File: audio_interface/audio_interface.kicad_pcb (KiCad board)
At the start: 2 copper layers, 137.8 x 66 mm, 153 parts, among them J1 XLR3, J10 MIC_EXT, J11 INST_EXT, J13 Test Headers, J14 SWD, J15 PCM_Jumper, J16 USB_B, J2 AudioJack2, J3 EXT_9V, J4 PROBE_GND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

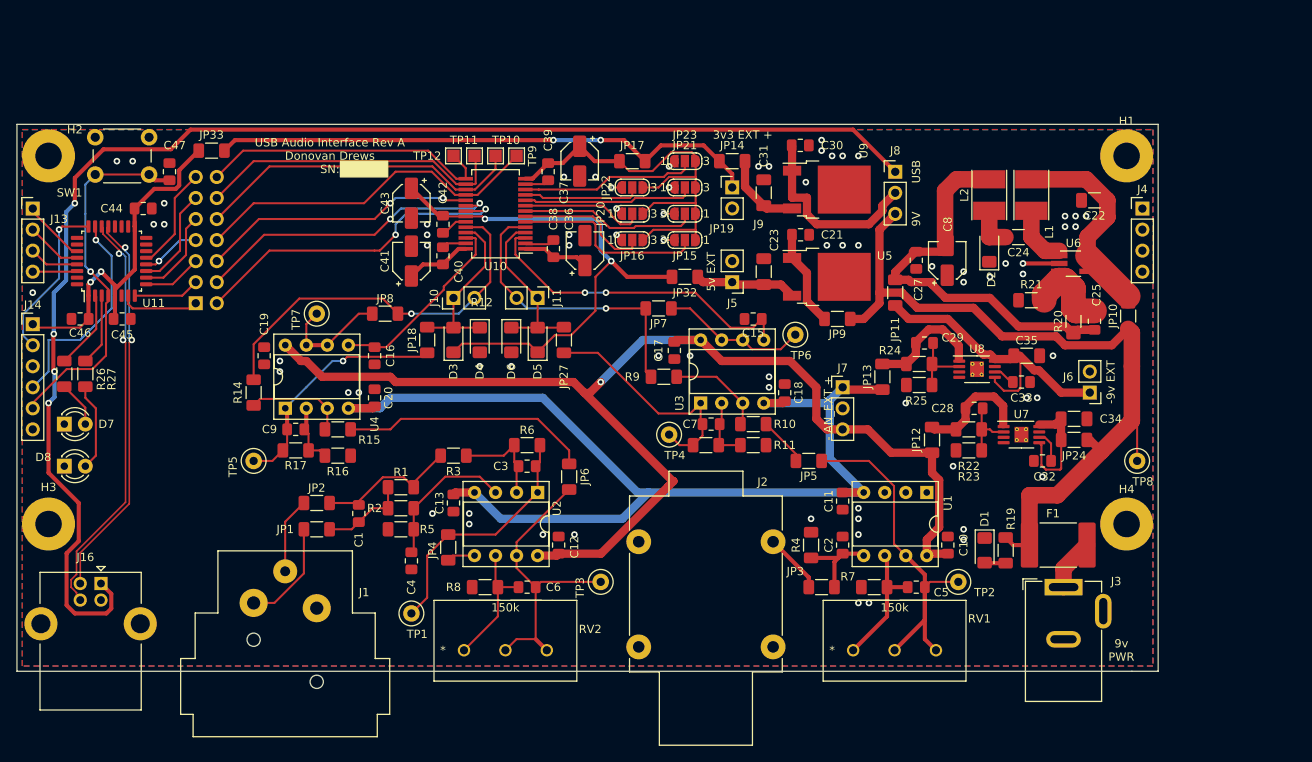
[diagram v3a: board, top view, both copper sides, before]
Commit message: Moved connectors to make flush with endplate. Ran DRC and fixed errors.
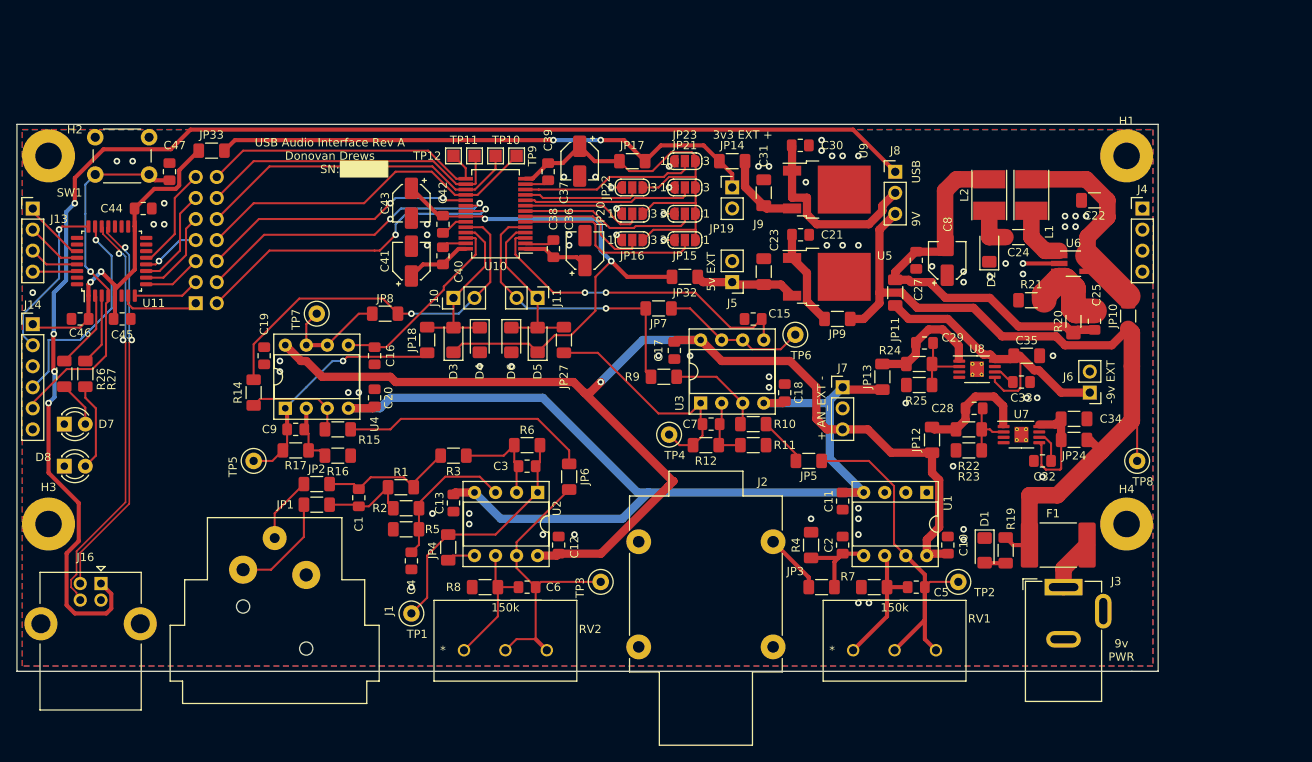
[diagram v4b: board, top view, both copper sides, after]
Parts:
- moved J1 4.21 mm to (147.3, 148.4)
- moved JP1 2.97 mm to (148.6, 139.9)
- moved JP2 2.29 mm to (148.6, 137.4)
- moved C1 1.91 mm to (153.7, 139.1)
- moved R2 0.63 mm to (159.4, 140.3)
- moved R5 0.63 mm to (159.4, 142.9)
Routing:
- net Net-(J1-Pad3): track 9.19 -> 7.98 mm
- net Net-(C1-Pad2): track 17.6 -> 16.7 mm
- net /Digital/ADC_3V3: track 55.9 -> 55.3 mm
- net Net-(C25-Pad1): track 50.9 -> 50.4 mm
- net GNDA: vias 72 -> 73
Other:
- board text added: "+ AN_EXT -"
- board text removed: "- AN_EXT +"

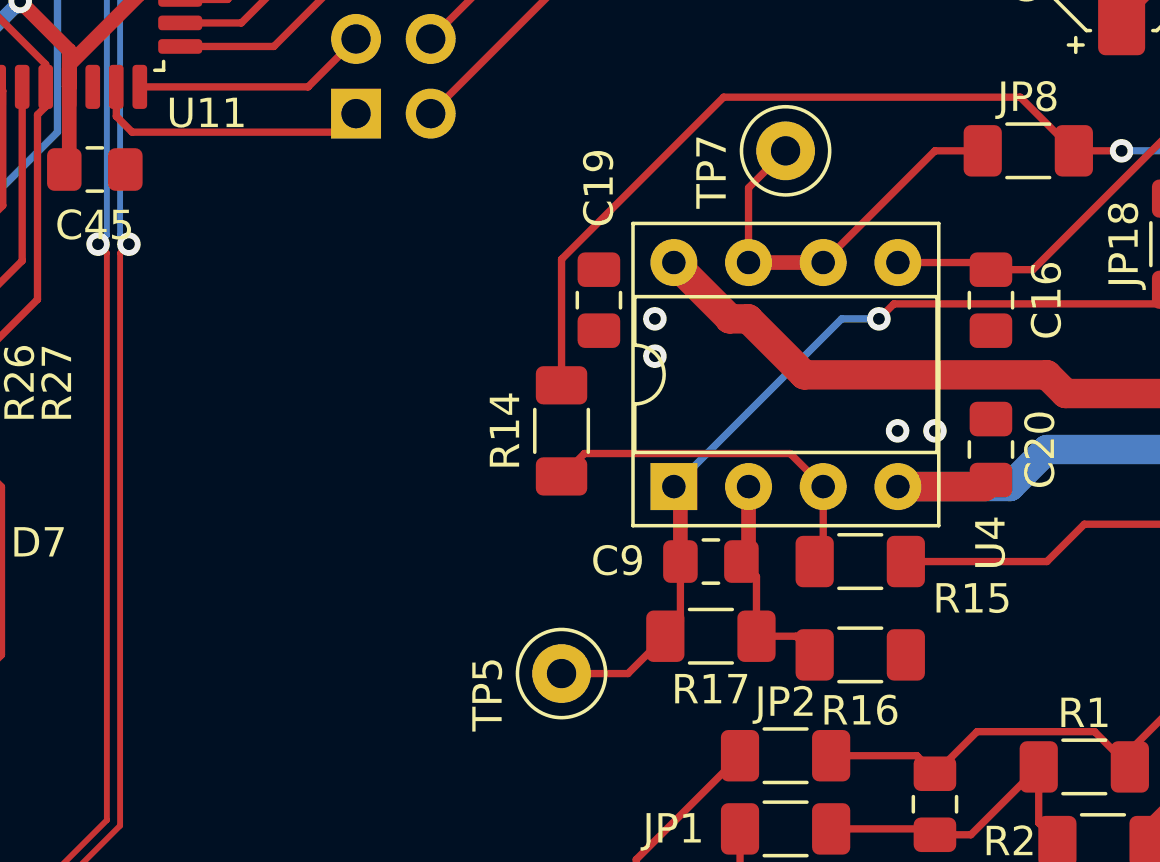
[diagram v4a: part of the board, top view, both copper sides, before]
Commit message: Small grounding improvements
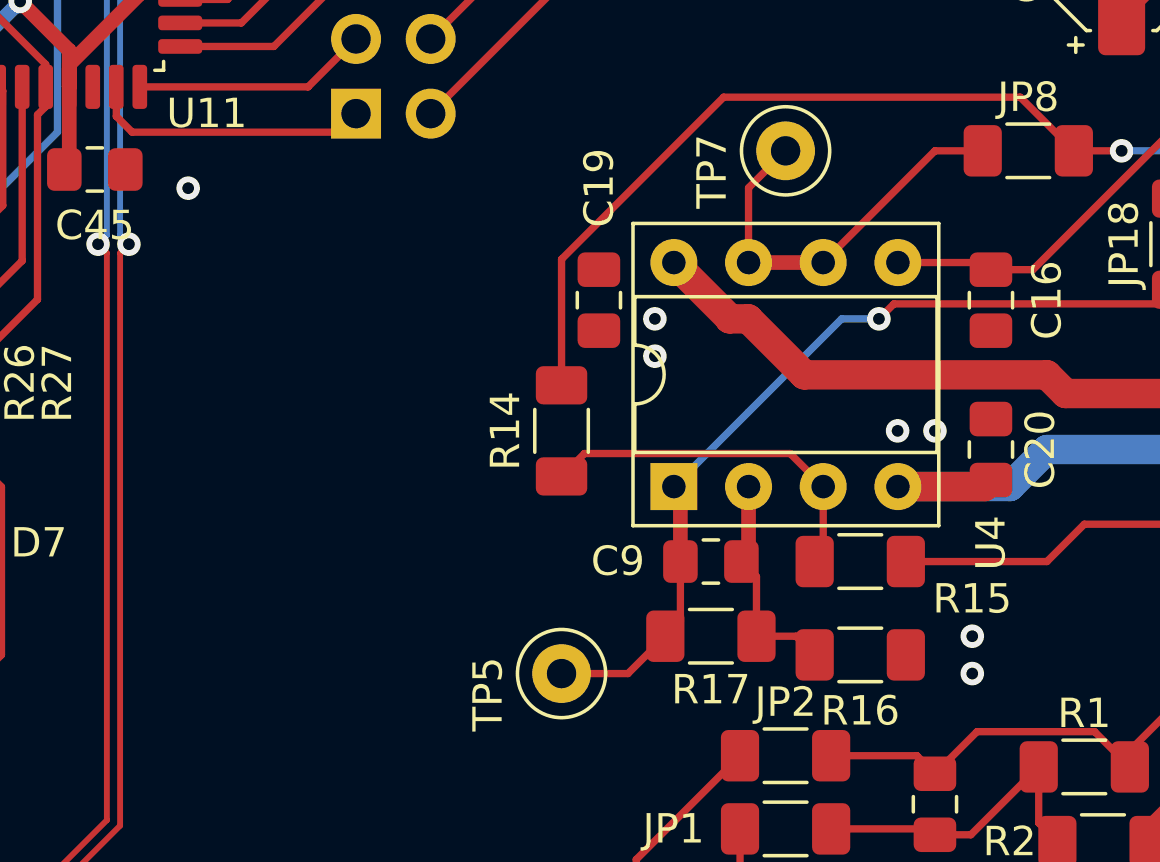
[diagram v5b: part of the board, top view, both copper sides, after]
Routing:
- net GNDA: vias 73 -> 76
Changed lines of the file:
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@@
     (property "Sheetfile" "power.kicad_sch")
     (property "Sheetname" "Power")
+    (zone_connect 2)
     (attr smd)
     (fp_text reference "U7" (at 0 -2.45) (layer "F.SilkS")
@@
   (via (at 201.93 99.06) (size 0.8) (drill 0.4) (layers "F.Cu" "B.Cu") (free) (net 4))
   (via (at 226.695 142.875) (size 0.8) (drill 0.4) (layers "F.Cu" "B.Cu") (free) (net 4))
+  (via (at 128.27 118.11) (size 0.8) (drill 0.4) (layers "F.Cu" "B.Cu") (free) (net 4))
   (via (at 203.2 125.73) (size 0.8) (drill 0.4) (layers "F.Cu" "B.Cu") (free) (net 4))
   (via (at 213.995 143.51) (size 0.8) (drill 0.4) (layers "F.Cu" "B.Cu") (free) (net 4))
@@
   (via (at 208.28 141.605) (size 0.8) (drill 0.4) (layers "F.Cu" "B.Cu") (free) (net 4))
   (via (at 161.925 106.045) (size 0.8) (drill 0.4) (layers "F.Cu" "B.Cu") (free) (net 4))
+  (via (at 154.94 134.62) (size 0.8) (drill 0.4) (layers "F.Cu" "B.Cu") (free) (net 4))
   (via (at 238.94548 105.06274) (size 0.8) (drill 0.4) (layers "F.Cu" "B.Cu") (free) (net 4))
   (via (at 189.865 121.92) (size 0.8) (drill 0.4) (layers "F.Cu" "B.Cu") (free) (net 4))
+  (via (at 154.94 133.35) (size 0.8) (drill 0.4) (layers "F.Cu" "B.Cu") (free) (net 4))
   (via (at 190.5 107.95) (size 0.8) (drill 0.4) (layers "F.Cu" "B.Cu") (free) (net 4))
   (via (at 130.175 106.045) (size 0.8) (drill 0.4) (layers "F.Cu" "B.Cu") (free) (net 4))

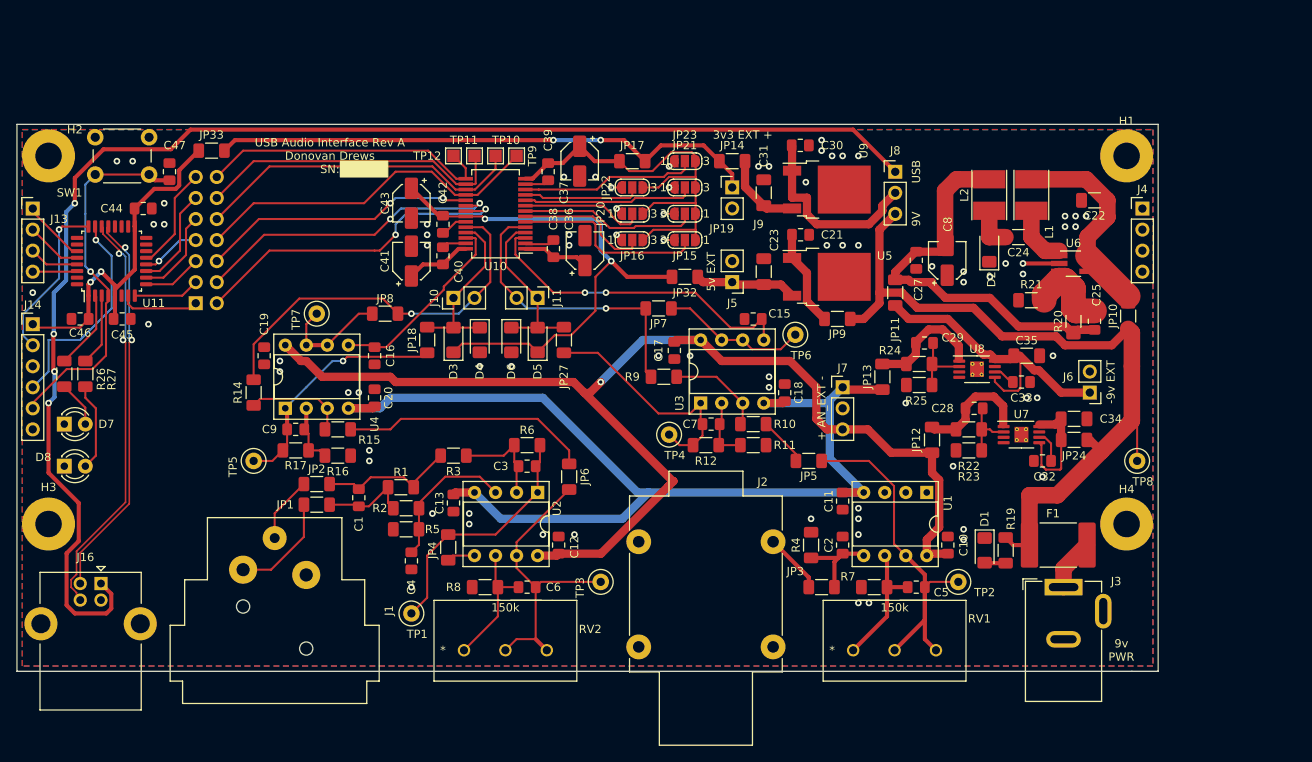
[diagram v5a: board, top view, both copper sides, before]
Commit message: Polygons for switching regulator. Silkscreen improvements,
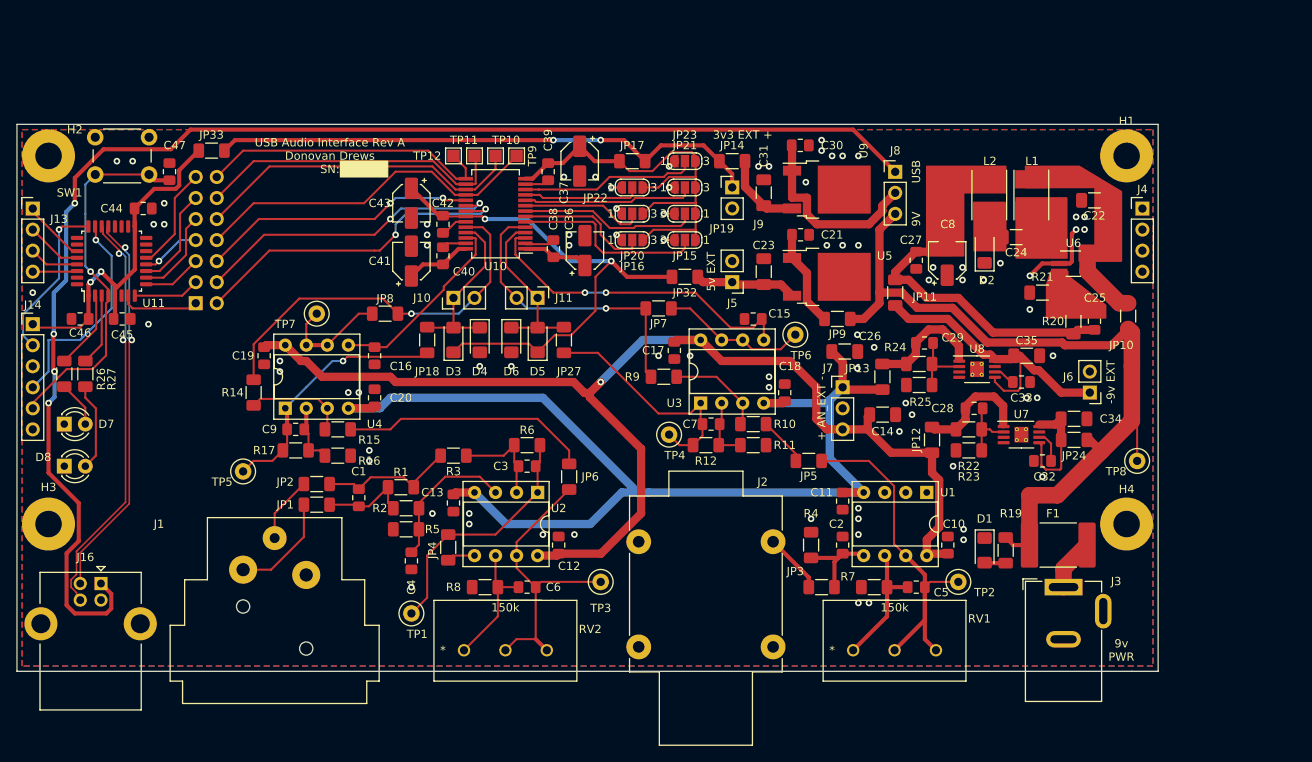
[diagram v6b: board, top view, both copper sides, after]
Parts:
- added C14: 1u, Capacitor_SMD:C_1206_3216Metric_Pad1.33x1.80mm_HandSolder, F.Cu at (216.9, 129.0)
- added C26: 1u, Capacitor_SMD:C_1206_3216Metric_Pad1.33x1.80mm_HandSolder, F.Cu at (212.3, 121.4)
- moved TP5 1.80 mm to (139.7, 135.9)
- moved R21 1.63 mm to (236.2, 114.3)
- moved D2 0.58 mm to (229.2, 109.2)
- moved C24 0.27 mm to (233.0, 107.6)
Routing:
- net GNDA: track 24.2 -> 29.7 mm, vias 76 -> 81
- net VSSA: track 130.3 -> 134.3 mm
- net Net-(C22-Pad1): track 24.8 -> 28.5 mm
- net Net-(C25-Pad2): track 10.4 -> 8.50 mm
- net /Digital/ADC_5V: track 64.9 -> 63.0 mm
- net MIC_OUT: track 29.4 -> 31.2 mm
- net Net-(C25-Pad1): track 50.4 -> 48.7 mm
- net VAA: track 145.6 -> 146.6 mm
- net Net-(C24-Pad2): track 5.14 -> 5.85 mm
- net Net-(C24-Pad1): track 7.24 -> 7.85 mm
